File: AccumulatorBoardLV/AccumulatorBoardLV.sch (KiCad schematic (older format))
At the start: 47 parts, among them J1 Contactor 1, J10 To HV Board, J11 IMD Reset, J12 TS Interlock, J13 Temp Reset, J14 To ECU, J15 Charger LV, J16 Charger Interlock, J17 Lid Interlock, J18 From HV Board, J19 Chip 1, J2 BMS Connector 1, J20 Chip 2, J21 Chip 3, J22 Chip 4, J3 BMS Connector 2, J4 BMS TX, J5 BMS RX, J6 Current Sensor, J7 Contactor 2, J8 IMD LV, J9 BMS Reset, U1 DE1A1B-L2-12V, U10 MCP3008, U11 ISO1050, U12 stm_nucleo_FK303K8, U13 MCP3008, U14 MCP3008, U2 LM555N, U3 SN754410, U4 DE1A1B-L2-12V, U5 L78S05CV-DG, U6 DE1A1B-L2-12V, U7 DK1A1B-12V, U8 ADUM4154ARIZ, U9 MCP3008

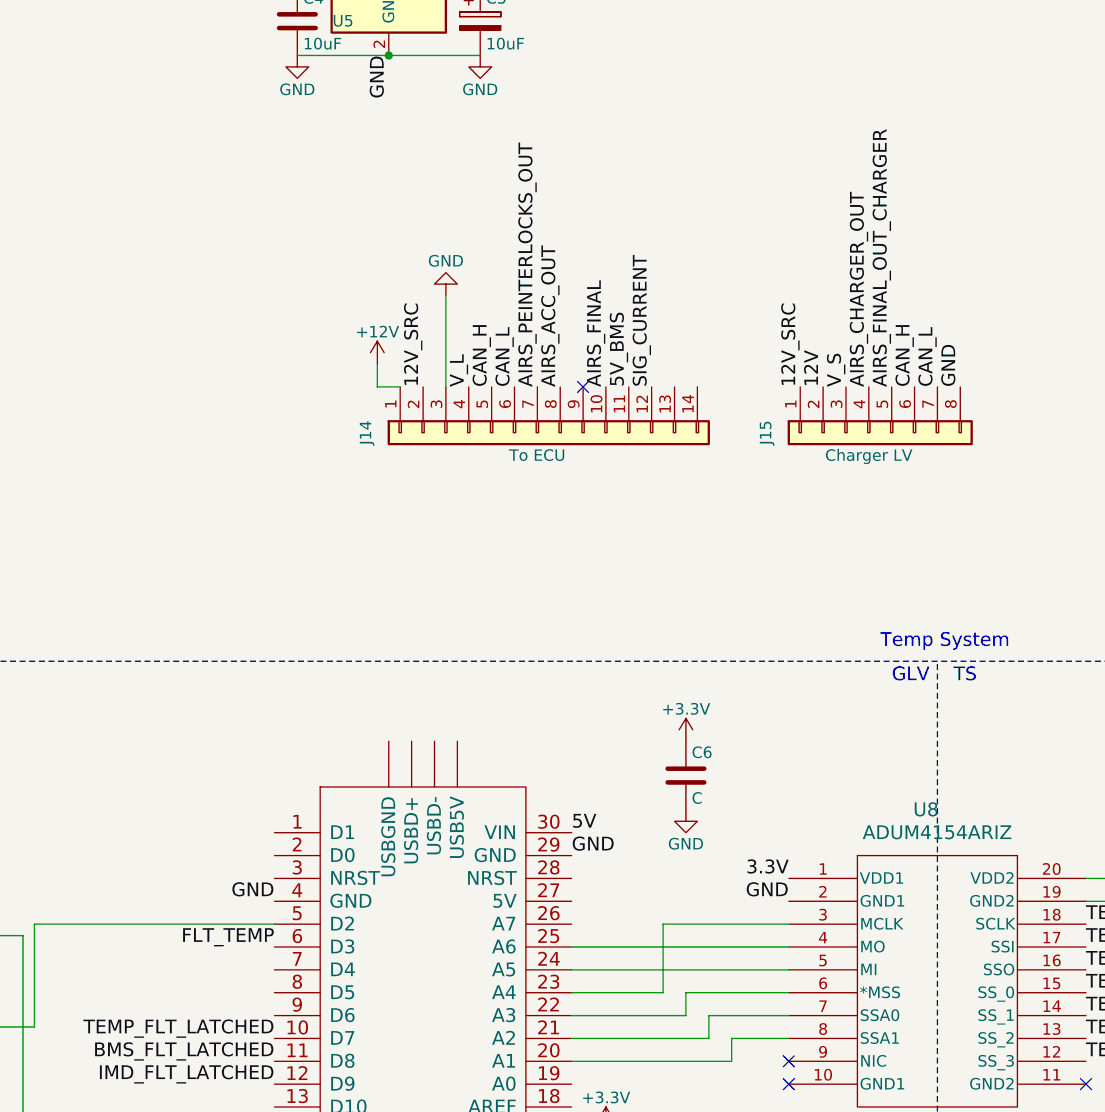
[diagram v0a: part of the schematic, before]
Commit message: Revise Accumulator HV and LV, route Dash Switchbox, begin PE HV
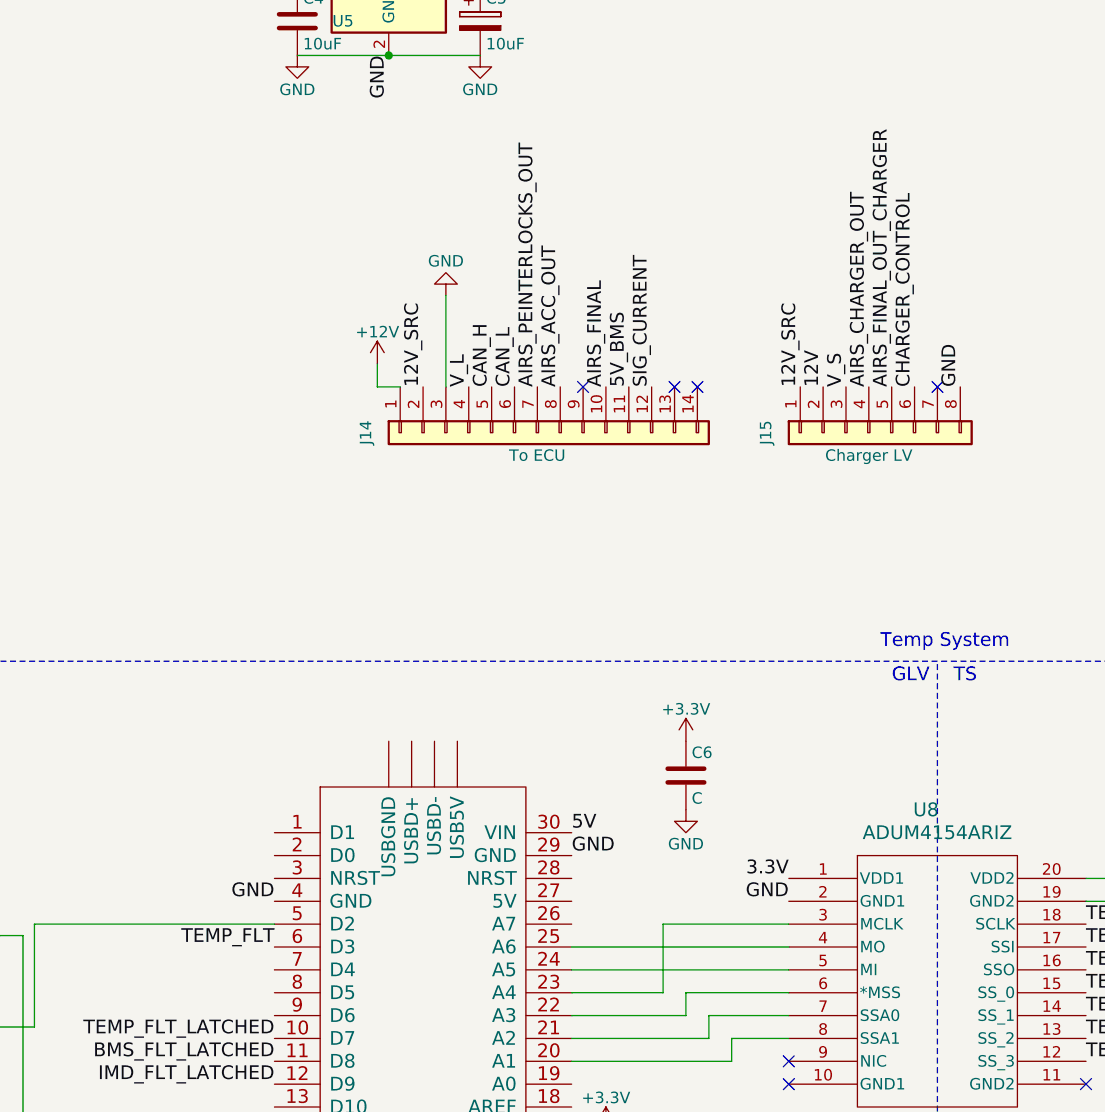
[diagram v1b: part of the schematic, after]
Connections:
- net FLT_TEMP is gone; now on net TEMP_FLT: U12.6 (D3)
- net CAN_H: no longer J15.6 (Pin_6)
- net CAN_L: no longer J15.7 (Pin_7)
- new net CHARGER_CONTROL: J15.6 (Pin_6)
- no-connect marks 8 -> 11
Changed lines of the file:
@@
 Text Label 6250 4700 1    60   ~ 0
 GND
-Text Label 6150 4700 1    60   ~ 0
-CAN_L
 Text Label 6050 4700 1    60   ~ 0
-CAN_H
+CHARGER_CONTROL
 Text Label 5950 4700 1    60   ~ 0
 AIRS_FINAL_OUT_CHARGER
@@
 $EndComp
 Text Label 3250 7150 2    60   ~ 0
-FLT_TEMP
+TEMP_FLT
 Wire Wire Line
 	11650 3350 11950 3350
@@
 Wire Wire Line
 	850  7450 850  7500
+NoConn ~ 6150 4700
+NoConn ~ 5000 4700
+NoConn ~ 5100 4700
 $EndSCHEMATC

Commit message: Re-layout Accumulator LV PCB, adding mounting holes
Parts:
- removed C6: C, Capacitors_THT:CP_Radial_D6.3mm_P2.50mm, symbol C
- added C6, C8: CP, Capacitors_THT:CP_Radial_D5.0mm_P2.50mm, symbol CP
- added H1, H2, H3: MtngHole, Mounting_Holes:MountingHole_4.5mm, symbol Conn_01x01
- C1, C2, C3, C4, C5, C7: footprint Capacitors_THT:CP_Radial_D6.3mm_P2.50mm -> Capacitors_THT:CP_Radial_D5.0mm_P2.50mm
- J10: footprint Connectors_Molex:Molex_NanoFit_1x04x2.50mm_Straight -> Connectors_Molex:Molex_NanoFit_2x02x2.50mm_Straight
- J2, J8: footprint Connectors_Molex:Molex_NanoFit_1x06x2.50mm_Straight -> Connectors_Molex:Molex_NanoFit_2x03x2.50mm_Straight
- R1, R2, R3, R4: footprint Resistors_THT:R_Axial_DIN0411_L9.9mm_D3.6mm_P12.70mm_Horizontal -> Resistors_THT:R_Axial_DIN0207_L6.3mm_D2.5mm_P10.16mm_Horizontal
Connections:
- net +3V3: now also C6.1
- net +5V: now also C8.1
- net GND: now also C6.2, C8.2

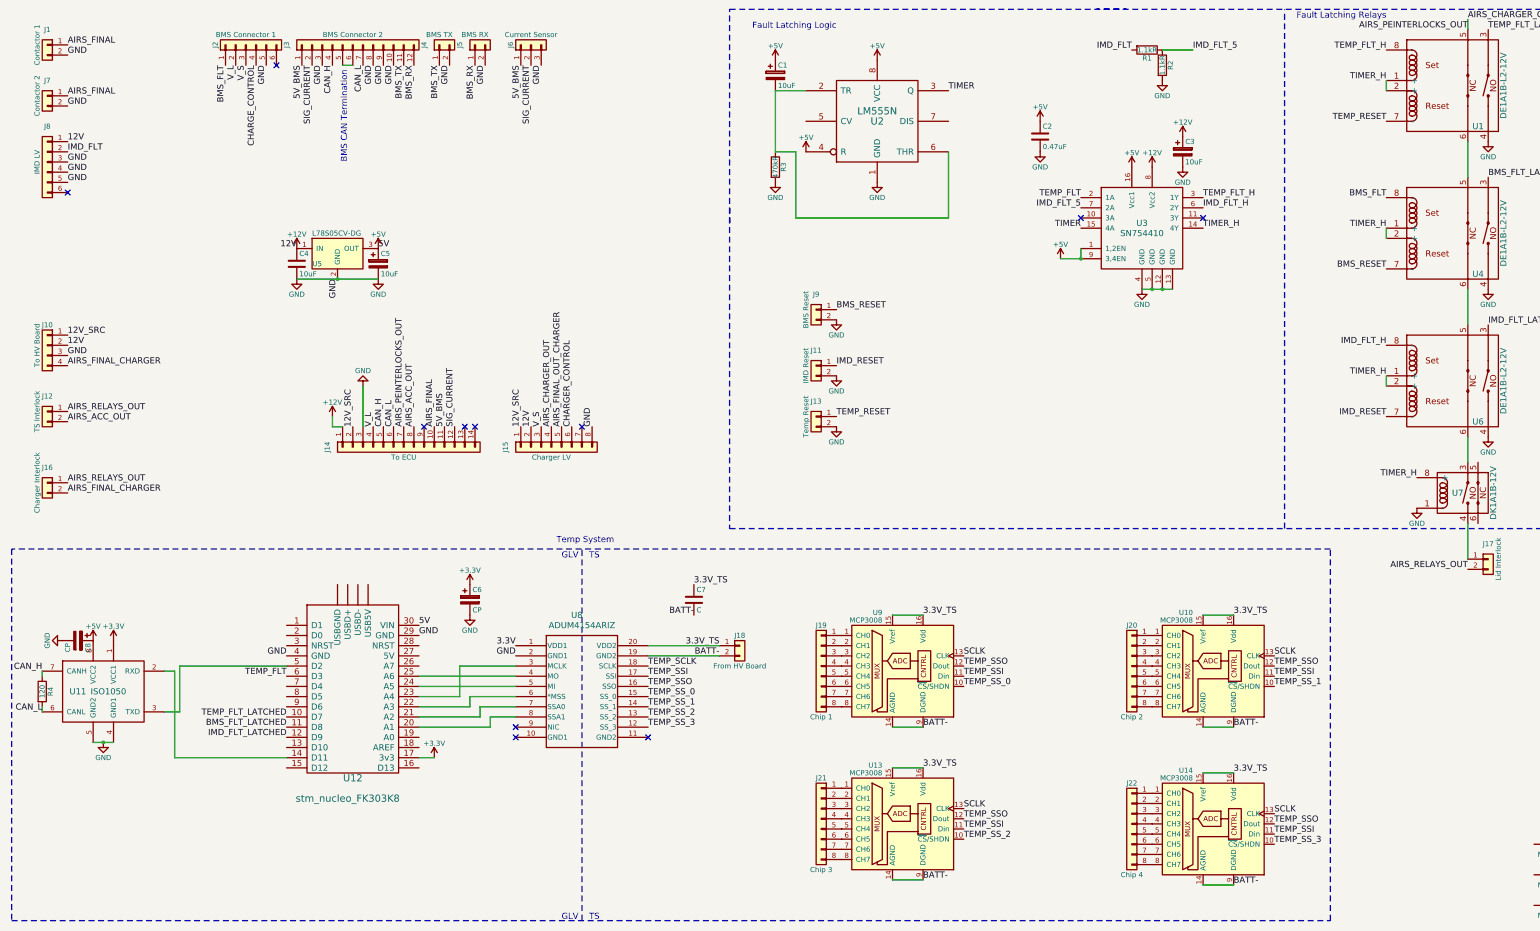
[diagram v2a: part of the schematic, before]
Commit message: Add planes to Accumulator LV board
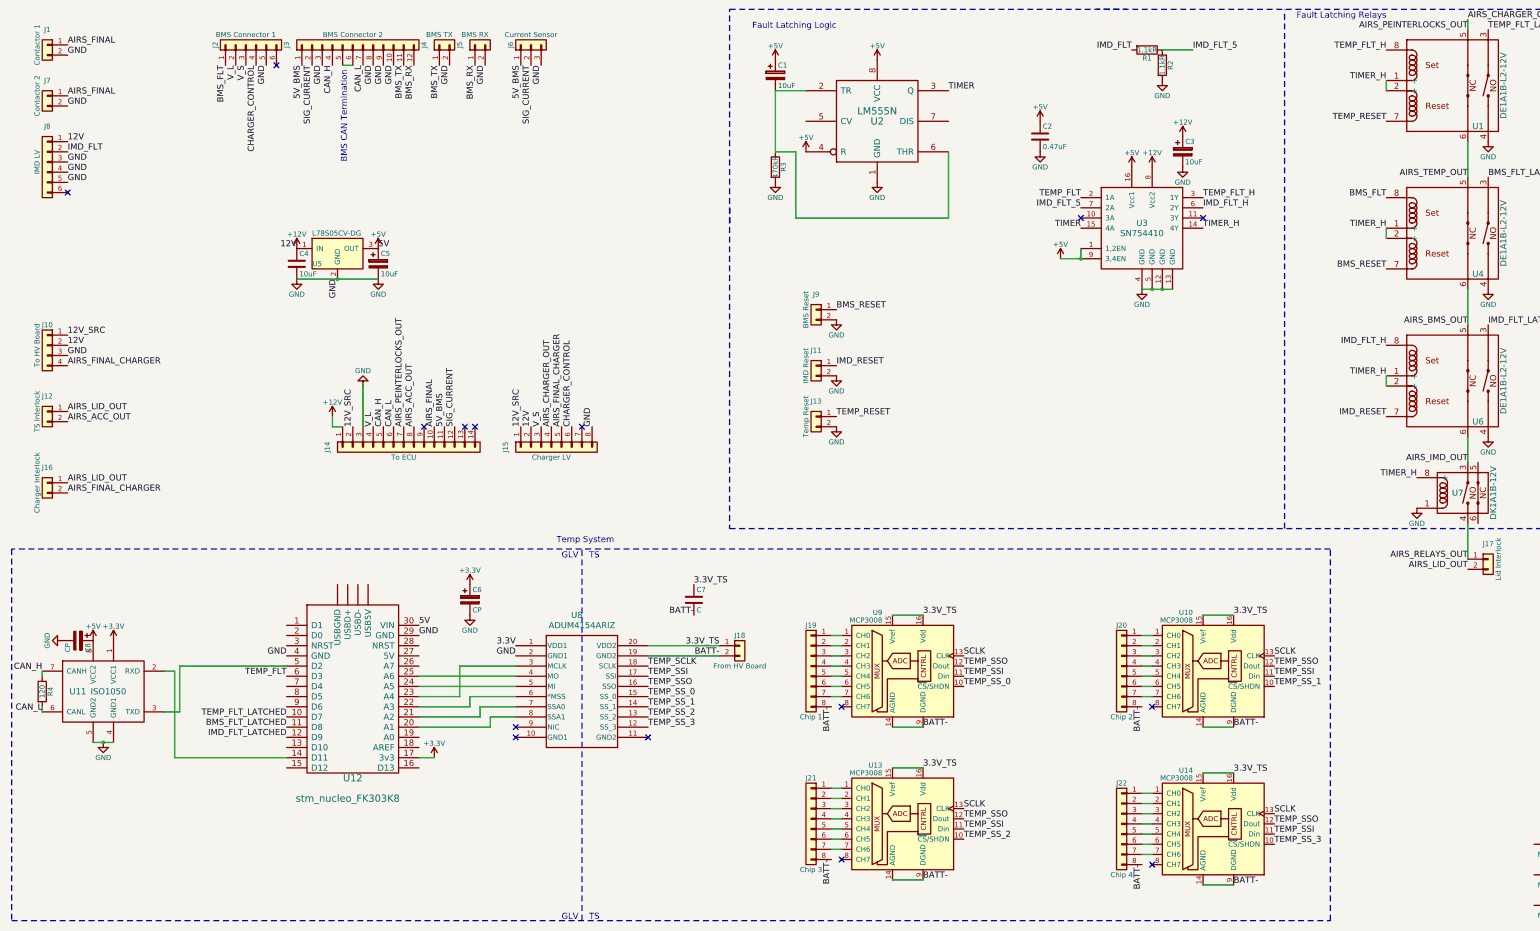
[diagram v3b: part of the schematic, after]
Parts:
- J19, J20, J21, J22: footprint Connectors_Molex:Molex_NanoFit_1x08x2.50mm_Straight -> Connectors_Molex:Molex_NanoFit_2x04x2.50mm_Straight
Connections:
- net AIRS_FINAL_OUT_CHARGER is gone; now on net AIRS_FINAL_CHARGER: J15.5 (Pin_5)
- net CHARGE_CONTROL is gone; now on net CHARGER_CONTROL: J2.4 (Pin_4)
- net AIRS_RELAYS_OUT: now also J17.1 (Pin_1), U7.4; no longer J12.1 (Pin_1), J16.1 (Pin_1), J17.2 (Pin_2)
- net BATT-: now also J19.8 (Pin_8), J20.8 (Pin_8), J21.8 (Pin_8), J22.8 (Pin_8)
- net AIRS_IMD_OUT: now reaches U6.6, U7.3
- net at U13.8 (CH7): no longer J21.8 (Pin_8)
- net at U10.8 (CH7): no longer J20.8 (Pin_8)
- net at U14.8 (CH7): no longer J22.8 (Pin_8)
- net at U9.8 (CH7): no longer J19.8 (Pin_8)
- net AIRS_TEMP_OUT: now reaches U1.6, U4.5
- net AIRS_BMS_OUT: now reaches U4.6, U6.5
- new net AIRS_LID_OUT: J12.1 (Pin_1), J16.1 (Pin_1), J17.2 (Pin_2)
- no-connect marks 11 -> 15
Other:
- moved on the sheet: J19, J20, J21, J22

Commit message: Create joined PCBs for manufacturing on the same board
Accumulator one is having problems with the exported files on DFM for some reason
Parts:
- U12: footprint arduino:arduino_mini -> FSFootprints:arduino_mini
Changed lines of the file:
@@
 F 0 "U12" H 3900 6850 70  0000 C CNN
 F 1 "stm_nucleo_FK303K8" H 3850 6650 70  0000 C CNN
-F 2 "arduino:arduino_mini" H 3950 6150 60  0001 C CNN
+F 2 "FSFootprints:arduino_mini" H 3950 6150 60  0001 C CNN
 F 3 "" H 4500 7650 60  0001 C CNN
 	1    3900 7500
